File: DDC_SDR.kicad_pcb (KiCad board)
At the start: 2 copper layers, 100 x 100 mm, 282 parts, among them J1 Filter, J11 SDR ANT, J13 AWG_OUT, J14 DUT, J15 OLED, J16 S21_OUT, J2 Filter, J3 Filter, J4 Filter, J5 Conn_01x02, J6 PMOD, J9 3.5mm_Jack, Q1 AO3401A, Q10 2N7002, Q3 2N7002, Q4 2N7002, Q5 2N7002, Q6 2N7002, Q7 2N7002, Q8 2N7002, Q9 2N7002, SW1 RotaryEncoder_Switch_MP, U10 74LVC1G3157GW, U11 74LVC1G3157GW, U12 PAM8908, U13 74LVC1G3157GW, U14 74LVC1G3157GW, U15 TPH2501-TR, U16 TPH2501-TR, U17 TPH2501-TR, U18 74LVC1G3157GW, U19 74LVC1G3157GW, U2 MS9280, U20 74LVC1G3157GW, U21 74LVC1G3157GW, U22 74LVC1G3157GW, U23 74LVC1G3157GW, U24 74LVC1G3157GW, U25 TPH2501-TR, U26 74LVC1G3157GW, U27 74LVC1G3157GW, U3 MS9708, U4 CJC4334H, U5 NCP115AMX120TCG, U6 L78M05ABDT-TR, U7 ICE40UP5K-SG48ITR, X1 SG-8018CE 30.720000MHz TJHPA

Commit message: Working on the analog chains
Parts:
- removed C103: 100nF, PCM_JLCPCB:C_0402
- removed R39: 510Ω, PCM_JLCPCB:R_0805
- added R85: 10Ω, PCM_JLCPCB:R_0402, F.Cu at (104.3, 105.0)
- R4, R41: footprint PCM_JLCPCB:R_0805 -> PCM_JLCPCB:R_0402
- R50: value 10Ω -> 510Ω; footprint PCM_JLCPCB:R_0603 -> PCM_JLCPCB:R_0402
- R51: footprint PCM_JLCPCB:R_0603 -> PCM_JLCPCB:R_0402
- moved C1 425.1 mm to (230.9, 61.7)
- moved C3 425.1 mm to (230.9, 63.5)
- moved C4 425.1 mm to (230.9, 65.4)
- moved C51 425.1 mm to (235.7, 65.4)
- moved C54 425.1 mm to (235.7, 67.2)
- moved C56 425.1 mm to (235.7, 69.1)
- moved C60 425.1 mm to (235.7, 71.0)
- moved D5 425.1 mm to (239.0, 70.1)
- moved J15 425.1 mm to (246.9, 63.1)
- moved JP1 425.1 mm to (239.3, 67.1)
- moved R1 425.1 mm to (230.9, 67.2)
- moved R12 425.1 mm to (238.6, 72.3)
- moved R2 425.1 mm to (230.9, 69.1)
- moved R3 425.1 mm to (230.9, 71.0)
- moved SW1 425.1 mm to (212.9, 65.9)
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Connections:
- C7 pad 2: /TX_OUT -> Net-(C7-Pad2)
- R50 pad 1: Net-(R50-Pad1) -> Net-(U16--)
- R50 pad 2: Net-(R48-Pad1) -> Net-(R50-Pad2)
- R51 pad 1: Net-(R48-Pad1) -> Net-(R51-Pad1)
- R51 pad 2: Net-(R51-Pad2) -> Net-(R48-Pad1)
- R58 pad 2: Net-(R50-Pad1) -> Net-(R58-Pad2)
- R74 pad 2: Net-(R39-Pad2) -> Net-(R50-Pad2)
- R81 pad 2: Net-(C103-Pad1) -> Net-(C7-Pad2)
- TP31 pad 1: Net-(R39-Pad2) -> Net-(R50-Pad2)
- U10 pad 1: Net-(R51-Pad2) -> Net-(R51-Pad1)
- U13 pad 1: Net-(R50-Pad1) -> Net-(R58-Pad2)
- U16 pad 1: Net-(R39-Pad2) -> Net-(R50-Pad2)
- U27 pad 4: Net-(C103-Pad1) -> Net-(C7-Pad2)
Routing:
- net VA/2: track 0.00 -> 19.2 mm

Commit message: AF DAC Some VDDA Placed
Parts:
- removed the R15 at (-199.9, 57.0)
- removed the R16 at (-199.9, 60.0)
- removed the R22 at (204.3, 157.4)
- removed the R31 at (204.3, 160.4)
- removed the R32 at (204.3, 163.3)
- removed the R33 at (204.3, 166.3)
- added C106: 100nF, PCM_JLCPCB:C_0402, F.Cu at (180.0, 120.1)
- added R23: 10kΩ, PCM_JLCPCB:R_0402, F.Cu at (-193.3, 57.8)
- added R24: 10kΩ, PCM_JLCPCB:R_0402, F.Cu at (-193.3, 59.6)
- added R49: 560Ω, PCM_JLCPCB:R_0603, F.Cu at (170.6, 118.5)
- added R50: 560Ω, PCM_JLCPCB:R_0603, F.Cu at (165.4, 121.6)
- added R82: 100kΩ, PCM_JLCPCB:R_0402, F.Cu at (106.9, 81.5)
- added R83: 100kΩ, PCM_JLCPCB:R_0402, F.Cu at (109.0, 77.1)
- added R85: 100kΩ, PCM_JLCPCB:R_0402, F.Cu at (101.7, 84.9)
- added R86: 100kΩ, PCM_JLCPCB:R_0402, F.Cu at (101.4, 87.1)
- added R89: 10kΩ, PCM_JLCPCB:R_0402, F.Cu at (168.4, 116.8)
- added R90: 10kΩ, PCM_JLCPCB:R_0402, F.Cu at (162.9, 122.0)
- JP6: renamed from JP3; moved to B.Cu
- TP7: renamed from TP8; moved to B.Cu
- TR1: renamed from TR4; footprint Intro_to_CAD:XFMR_H1102NLT -> Transformer_SMD:Transformer_Ethernet_Wuerth_749013011A
- TR2: renamed from TR3; footprint Intro_to_CAD:XFMR_H1102NLT -> Transformer_SMD:Transformer_Ethernet_Wuerth_749013011A
- TR3: renamed from TR2; footprint Intro_to_CAD:XFMR_H1102NLT -> Transformer_SMD:Transformer_Ethernet_Wuerth_749013011A
- TR4: renamed from TR1; footprint Intro_to_CAD:XFMR_H1102NLT -> Transformer_SMD:Transformer_Ethernet_Wuerth_749013011A
- e3: renamed from e2; moved to B.Cu
- e4: renamed from e3; moved to B.Cu
- moved C60 75.9 mm to (165.7, 116.2)
- moved C59 72.4 mm to (161.3, 119.8)
- moved U9 70.1 mm to (160.2, 115.1)
- moved FB7 67.9 mm to (165.8, 113.2)
- moved C58 66.3 mm to (166.8, 119.0)
- moved R53 65.5 mm to (194.1, 116.7), turned to 90 degrees
- moved TP8 60.9 mm to (191.1, 117.5)
- moved C43 60.2 mm to (175.9, 103.8)
- moved U10 59.6 mm to (179.5, 123.2)
- moved e4 59.4 mm to (192.4, 121.8)
- moved e1 59.3 mm to (171.8, 102.2), turned to 180 degrees
- moved C61 59.0 mm to (170.6, 116.1), turned to 90 degrees
- moved FB4 57.5 mm to (169.4, 97.2), turned to 180 degrees
- moved e3 56.8 mm to (183.6, 120.1)
- moved JP6 55.8 mm to (183.6, 117.5)
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- renumbered A2 to A1, C98 to C1, C29 to C10, C76 to C100, C13 to C101, C68 to C102, C75 to C103, C105 to C104, C104 to C105, C28 to C11, C15 to C12, C107 to C13, C20 to C14, C19 to C15, C44 to C16, C21 to C17, C100 to C18, C7 to C19, C30 to C2, C101 to C20, C22 to C21, C102 to C22, C38 to C23, C109 to C24, C93 to C25, C23 to C26, C32 to C27, C84 to C28, C91 to C29, C99 to C3, C63 to C30, C34 to C31, C18 to C32, C64 to C33, C97 to C34, C106 to C35, C16 to C36, C65 to C37, C2 to C38, C42 to C39, C66 to C4, C5 to C40, C85 to C42, C55 to C43, C86 to C44, C43 to C45, C40 to C46, C87 to C47, C35 to C48, C88 to C49, C9 to C5, C17 to C50, C89 to C51, C36 to C52, C90 to C53, C37 to C54, C92 to C55, C48 to C56, C12 to C57, C46 to C58, C47 to C59, C52 to C6, C45 to C60, C49 to C61, C53 to C62, C58 to C63, C59 to C64, C26 to C65, C24 to C66, C25 to C67, C57 to C68, C50 to C69, C67 to C7, C62 to C70, C61 to C71, C54 to C72, C39 to C73, C60 to C74, C33 to C75, C51 to C76, C56 to C77, C1 to C78, C3 to C79, C31 to C8, C4 to C80, C70 to C81, C78 to C82, C69 to C83, C79 to C84, C73 to C85, C94 to C86, C74 to C87, C80 to C88, C95 to C89, C8 to C9, C81 to C90, C71 to C91, C82 to C92, C72 to C93, C83 to C94, C14 to C95, C6 to C96, C77 to C97, C10 to C98, C11 to C99, D7 to D1, D8 to D2, D6 to D3, D2 to D5, D1 to D6, D3 to D7, D5 to D8, FB2 to FB1, FB6 to FB2, FB8 to FB3, FB5 to FB4, FB9 to FB5, FB10 to FB6, J3 to J1, J11 to J10, J1 to J11, J2 to J12, J14 to J2, J4 to J3, J16 to J4, J13 to J5, J5 to J7, J15 to J8, JP51 to JP1, JP4 to JP2, JP52 to JP3, JP50 to JP4, JP2 to JP5, JP1 to JP7, Q10 to Q1, Q3 to Q2, Q1 to Q3, Q7 to Q4, Q6 to Q5, Q8 to Q6, Q9 to Q7, Q5 to Q8, Q4 to Q9, R59 to R1, R36 to R10, R60 to R11, R37 to R12, R35 to R13, R61 to R14, R62 to R15, R4 to R16, R68 to R17, R81 to R18, R82 to R19, R64 to R2, R67 to R20, R18 to R21, R8 to R22, R71 to R25, R70 to R26, R72 to R27, R69 to R28, R55 to R29, R79 to R3, R80 to R30, R14 to R31, R30 to R32, R83 to R33, R11 to R34, R84 to R35, R23 to R36, R13 to R37, R28 to R38, R21 to R39, R65 to R4, R6 to R40, R10 to R41, R5 to R42, R24 to R43, R7 to R44, R20 to R45, R25 to R46, R73 to R47, R34 to R48, R63 to R5, R19 to R53, R12 to R54, R1 to R55, R2 to R56, R3 to R57, R45 to R58, R75 to R59, R66 to R6, R38 to R60, R26 to R61, R50 to R62, R74 to R63, R44 to R64, R58 to R65, R85 to R66, R48 to R67, R27 to R68, R51 to R69, R9 to R7, R46 to R70, R57 to R71, R49 to R72, R53 to R73, R54 to R74, R29 to R75, R52 to R76, R47 to R77, R40 to R78, R56 to R79, R76 to R8, R41 to R80, R78 to R81, R43 to R84, R77 to R87, R42 to R88, R17 to R9, TP29 to TP1, TP31 to TP10, TP32 to TP11, TP10 to TP12, TP12 to TP13, TP30 to TP2, TP13 to TP3, TP25 to TP4, TP26 to TP5, TP27 to TP6, TP9 to TP8, TP28 to TP9, U26 to U1, U12 to U10, U5 to U11, U19 to U12, U16 to U13, U20 to U14, U13 to U15, U10 to U16, U21 to U17, U22 to U18, U23 to U19, U15 to U2, U17 to U20, U24 to U21, U11 to U22, U14 to U23, U18 to U24, U25 to U3, U2 to U4, U3 to U5, U27 to U6, U6 to U8, U4 to U9, e4 to e2
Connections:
- C26 pad 1: GNDA -> GND
- C29 pad 2: GNDA -> GND
- C31 pad 1: GNDA -> GND
- C48 pad 2: GNDA -> GND
- C49 pad 2: GNDA -> GND
- C50 pad 2: GNDA -> GND
- C51 pad 2: GNDA -> GND
- C52 pad 2: GNDA -> GND
- C53 pad 2: GNDA -> GND
- C54 pad 2: GNDA -> GND
- C57 pad 2: GNDA -> GND
- C60 pad 2: GNDA -> GND
- C61 pad 2: GNDA -> GND
- C62 pad 2: GNDA -> GND
- C63 pad 2: GNDA -> GND
- C64 pad 2: GNDA -> GND
- C65 pad 2: GNDA -> GND
- C67 pad 2: GNDA -> GND
- C68 pad 2: GNDA -> GND
- C69 pad 1: GNDA -> GND
- R40 pad 2: GNDA -> GND
- R41 pad 2: GNDA -> GND
- R53 pad 2: GNDA -> GND
- U10 pad 10: GNDA -> GND
- U10 pad 15: GNDA -> GND
- U10 pad 17: GNDA -> GND
- U9 pad 6: GNDA -> GND
- e4 pad 1: GNDA -> GND
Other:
- copper layers 2 -> 4

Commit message: SMA/LogicAnalyzer and VDDA placed
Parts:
- J2: value DUT -> S11; footprint Intro_to_CAD:Conn_Coaxial_Frohne -> Connector_Coaxial:SMA_Amphenol_132289_EdgeMount
- J4: footprint Intro_to_CAD:Conn_Coaxial_Frohne -> Connector_Coaxial:SMA_Amphenol_132289_EdgeMount
- JP5: moved to B.Cu
- moved C30 271.8 mm to (71.5, 122.0)
- moved C33 271.8 mm to (71.5, 123.8)
- moved C37 271.8 mm to (71.5, 125.7)
- moved R17 271.8 mm to (80.0, 122.0)
- moved R20 271.8 mm to (80.0, 120.1)
- moved R21 271.8 mm to (77.2, 120.1)
- moved R22 271.8 mm to (74.3, 129.3)
- moved R23 271.8 mm to (71.6, 118.8)
- moved R24 271.8 mm to (71.6, 120.6)
- moved R25 271.8 mm to (80.0, 127.5)
- moved R26 271.8 mm to (80.0, 125.7)
- moved R27 271.8 mm to (80.0, 129.3)
- moved R28 271.8 mm to (80.0, 123.8)
- moved R29 271.8 mm to (77.2, 127.5)
- moved R30 271.8 mm to (82.9, 114.5)
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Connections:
- U7 pad 18: /PMOD_0 -> /PMOD_2
- U7 pad 21: /PMOD_2 -> /PMOD_0
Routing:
- net VA/2: track 19.2 -> 0.00 mm

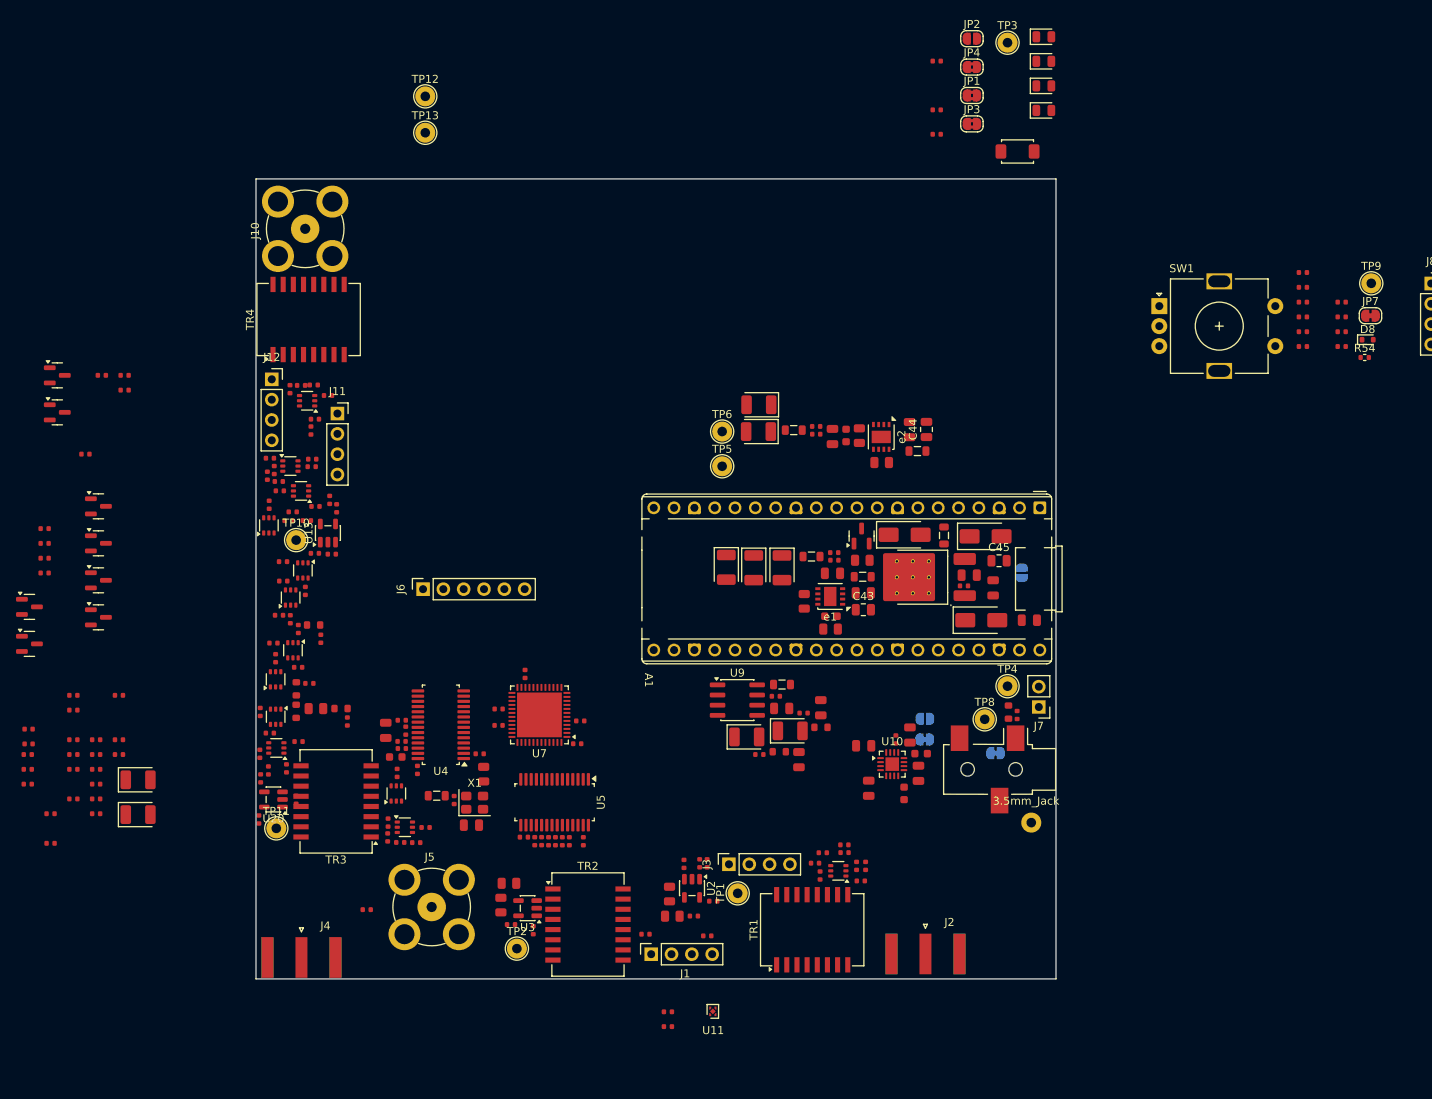
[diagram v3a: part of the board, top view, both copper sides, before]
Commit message: FPGA 1.2V placed
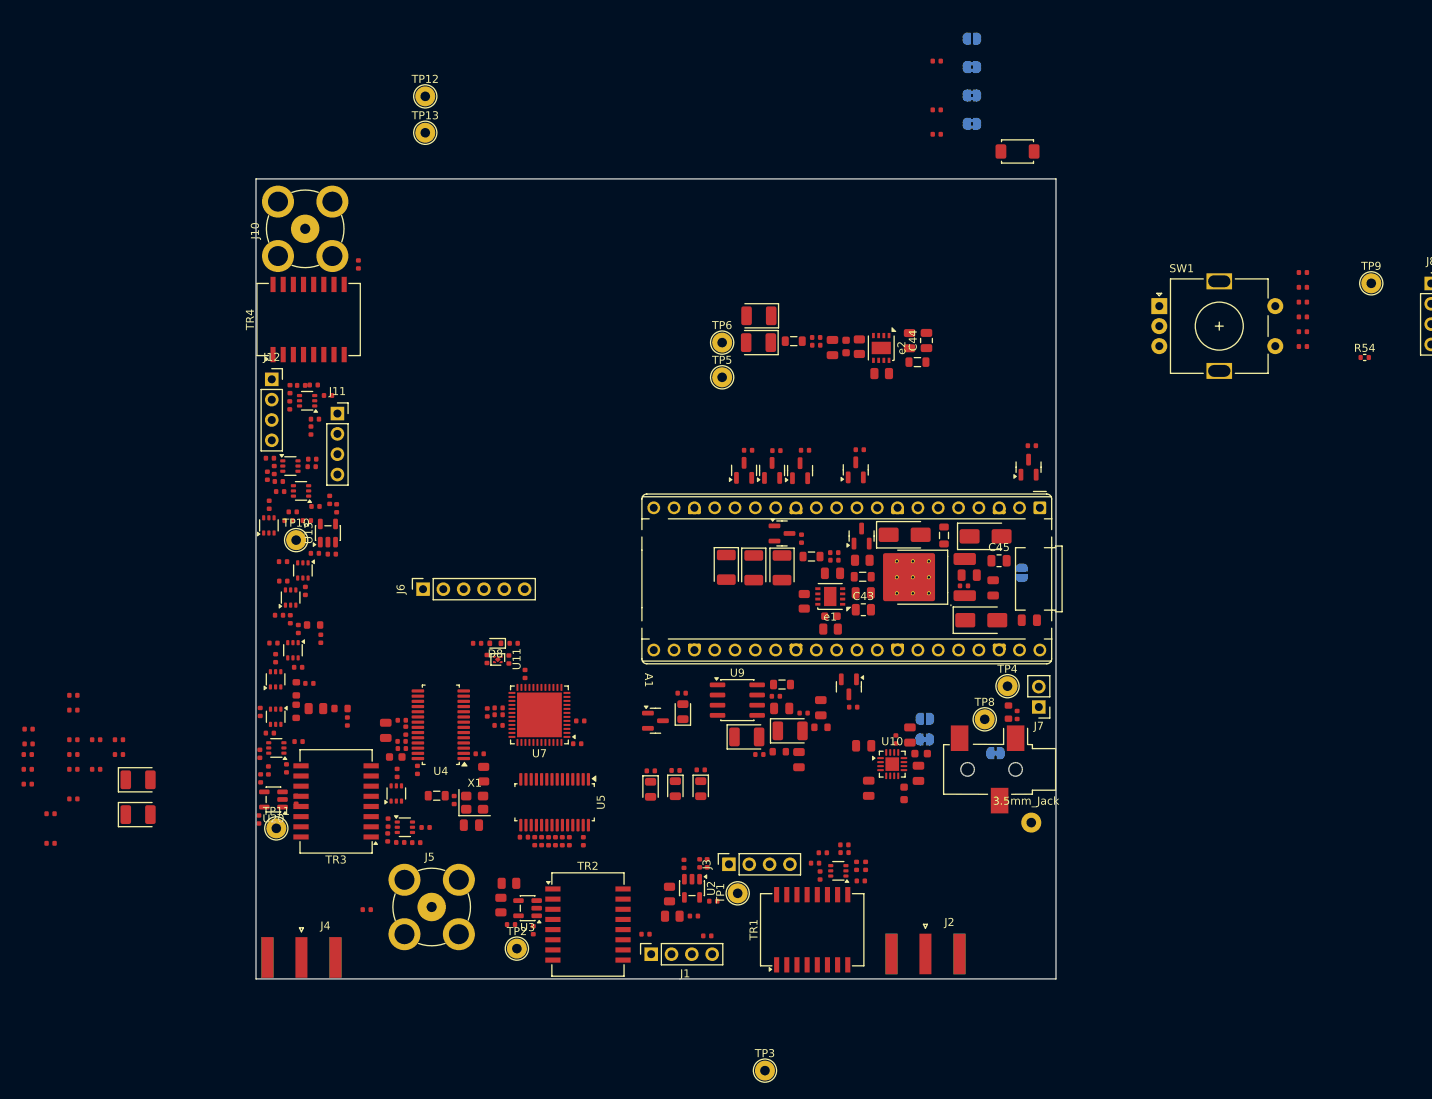
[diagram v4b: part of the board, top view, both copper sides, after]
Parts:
- removed JP7: Jumper_2_Bridged, Jumper:SolderJumper-2_P1.3mm_Bridged_RoundedPad1.0x1.5mm
- JP1, JP2, JP3, JP4: moved to B.Cu
- moved TP3 132.0 mm to (163.6, 161.5)
- moved Q9 122.0 mm to (196.6, 86.0), turned to 90 degrees
- moved C76 117.3 mm to (130.3, 117.0), turned to 180 degrees
- moved C77 116.9 mm to (128.9, 116.7), turned to -90 degrees
- moved C72 115.5 mm to (127.6, 108.0), turned to 180 degrees
- moved D8 115.5 mm to (129.9, 108.0), turned to 180 degrees
- moved R88 113.7 mm to (197.0, 83.3), turned to 180 degrees
- moved C74 109.9 mm to (132.2, 108.0)
- moved Q1 102.6 mm to (174.1, 113.5), turned to -90 degrees
- moved R64 102.4 mm to (175.5, 83.8), turned to 180 degrees
- moved D1 100.7 mm to (149.3, 126.3), turned to -90 degrees
- moved D3 100.5 mm to (155.6, 126.2), turned to -90 degrees
- moved D2 96.5 mm to (152.4, 126.2), turned to -90 degrees
- moved R70 96.0 mm to (168.6, 83.9), turned to 180 degrees
- moved D4 95.7 mm to (153.4, 116.6), turned to 90 degrees
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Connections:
- C73 pad 1: /FPGA Power/+1.2V_CORE -> +1V2
- C76 pad 1: /FPGA Power/+1.2V_CORE -> +1V2
- U7 pad 30: /FPGA Power/+1.2V_CORE -> +1V2
- U7 pad 5: /FPGA Power/+1.2V_CORE -> +1V2

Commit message: Fixed schematic errors, all placed
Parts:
- removed JP1: GBIN_PMOD_3, Jumper:SolderJumper-2_P1.3mm_Bridged2Bar_RoundedPad1.0x1.5mm
- moved R36 118.4 mm to (190.4, 87.4), turned to -90 degrees
- moved R22 116.3 mm to (182.8, 87.3), turned to 90 degrees
- moved R54 115.2 mm to (130.2, 111.4)
- moved R37 114.1 mm to (188.0, 87.3), turned to -90 degrees
- moved R34 112.7 mm to (177.4, 87.5), turned to -90 degrees
- moved TP9 111.2 mm to (137.1, 106.5)
- moved C79 110.7 mm to (125.6, 97.9), turned to -90 degrees
- moved R56 108.2 mm to (126.6, 97.9), turned to 90 degrees
- moved R33 107.6 mm to (185.3, 87.3), turned to -90 degrees
- moved R21 106.9 mm to (178.9, 87.3)
- moved R32 106.1 mm to (182.7, 112.5), turned to -90 degrees
- moved C78 104.6 mm to (132.8, 97.9), turned to -90 degrees
- moved R57 102.7 mm to (131.8, 97.9), turned to 90 degrees
- moved C80 100.0 mm to (131.7, 78.1), turned to 90 degrees
- moved R55 98.6 mm to (132.8, 78.1), turned to -90 degrees
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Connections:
- J6 pad 4: Net-(J6-Pin_4) -> /PMOD_3

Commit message: First wiring
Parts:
- moved C22 10.4 mm to (117.7, 123.5), turned to -90 degrees
- moved C15 9.57 mm to (143.0, 131.7), turned to -90 degrees
- moved C20 9.34 mm to (115.7, 115.7), turned to 180 degrees
- moved C12 9.30 mm to (117.3, 113.0), turned to 90 degrees
- moved R16 9.10 mm to (143.5, 130.1), turned to 0 degrees
- moved C23 8.88 mm to (143.6, 124.3), turned to 0 degrees
- moved C14 8.59 mm to (143.5, 129.3), turned to 180 degrees
- moved C16 8.47 mm to (120.6, 111.7), turned to 180 degrees
- moved R7 8.25 mm to (143.6, 128.4), turned to 0 degrees
- moved C21 8.24 mm to (143.6, 125.8), turned to 0 degrees
- moved R9 8.06 mm to (143.6, 127.5), turned to 0 degrees
- moved C18 8.05 mm to (143.6, 126.7), turned to 0 degrees
- moved C17 7.48 mm to (118.4, 113.7), turned to 90 degrees
- moved R29 6.72 mm to (131.3, 112.7), turned to 180 degrees
- moved C11 6.70 mm to (119.3, 113.7), turned to 90 degrees
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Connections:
- net /OA renamed /O+
- net /OB renamed /O-
- net Net-(TR3-RD+) renamed /A-
- net Net-(TR3-RD-) renamed /A+
- C61 pad 2: GND -> GNDA
- C67 pad 2: GND -> GNDA
- J4 pad 2: unconnected-(J4-Ext-Pad2) -> GND
- JP2 pad 1: /PMOD0 -> /PMOD_0
- R29 pad 1: Net-(U7A-IOT_46b_G0) -> Net-(U7A-IOT_37a)
- R89 pad 2: GND -> GNDA
- U10 pad 10: GND -> GNDA
- U10 pad 15: GND -> GNDA
- U10 pad 17: GND -> GNDA
- U7 pad 2: /DB5 -> /DB2
- U7 pad 23: /D7 -> Net-(U7A-IOT_37a)
- U7 pad 25: /D6 -> /D0
- U7 pad 26: /D5 -> /D1
- U7 pad 27: /D4 -> /D2
- U7 pad 28: /D2 -> /D3
- U7 pad 3: /DB6 -> /DB1
- U7 pad 31: /D3 -> /D4
- U7 pad 32: /D1 -> /D5
- U7 pad 34: /D0 -> /D6
- U7 pad 35: Net-(U7A-IOT_46b_G0) -> /D7
- U7 pad 4: /DB7 -> /DB0
- U7 pad 44: /DB0 -> /DB7
- U7 pad 45: /DB1 -> /DB6
- U7 pad 46: /DB2 -> /DB5
- U7 pad 47: /DB3 -> /DB4
- U7 pad 48: /DB4 -> /DB3
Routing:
- net /O+: track 0.00 -> 20.4 mm
- net /D0: track 0.00 -> 15.7 mm
- net /DB0: track 0.00 -> 15.5 mm
- net /D1: track 0.00 -> 14.7 mm
- net /DB1: track 0.00 -> 14.3 mm
- net /O-: track 0.00 -> 14.3 mm
- net /D2: track 0.00 -> 13.9 mm
- net /D3: track 0.00 -> 13.2 mm
- net /A-: track 0.00 -> 12.8 mm
- net /D4: track 0.00 -> 12.0 mm
- net /A+: track 0.00 -> 11.3 mm
- net /DB2: track 0.00 -> 11.3 mm
- net /D5: track 0.00 -> 11.1 mm
- net /D6: track 0.00 -> 9.96 mm
- net /DAC_CLK: track 0.00 -> 9.30 mm
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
